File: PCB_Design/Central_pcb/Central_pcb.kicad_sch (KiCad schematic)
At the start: 12 parts, among them U3 NRF52832-QFAA-R, Y1 CX2016DB32000D0WZRC1

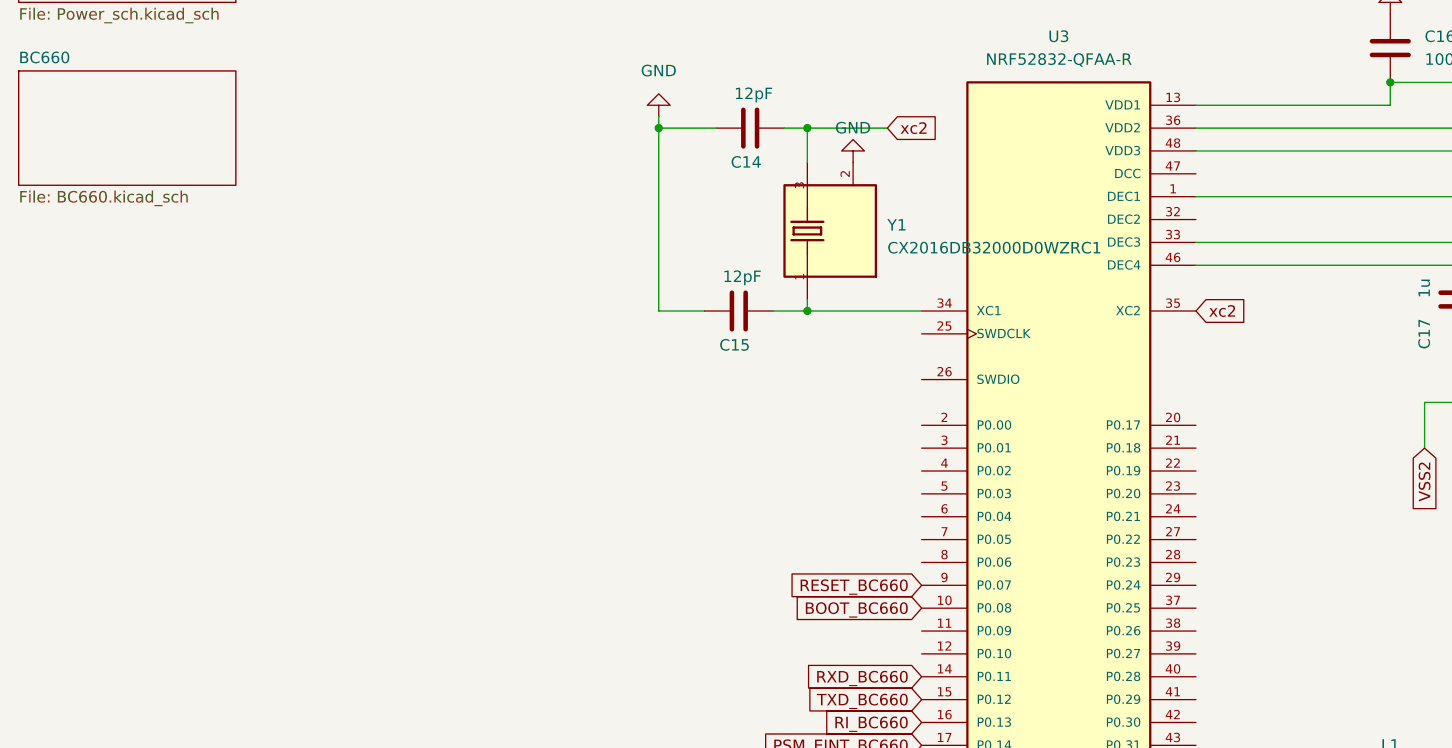
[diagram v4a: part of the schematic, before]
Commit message: Added debug conn
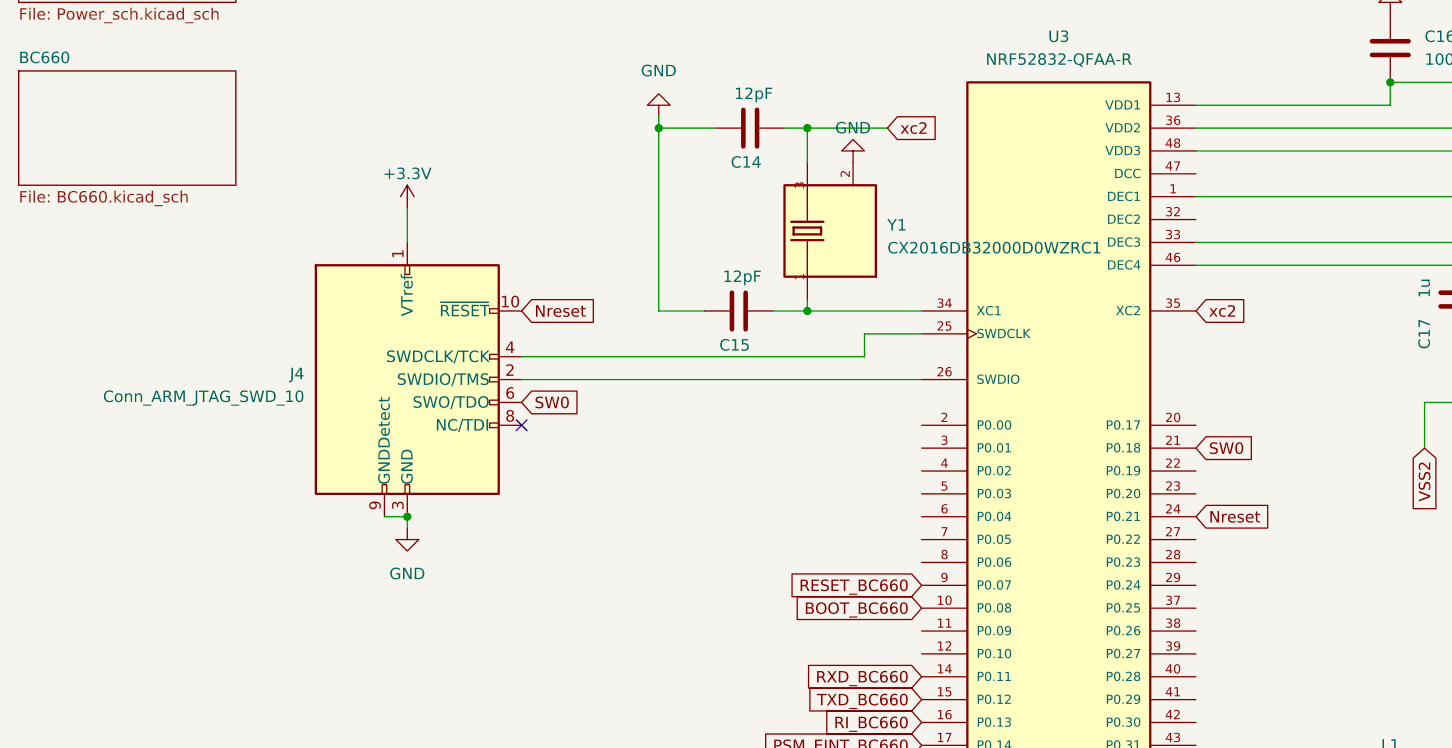
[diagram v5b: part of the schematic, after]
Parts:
- added J4: Conn_ARM_JTAG_SWD_10, Connector_PinSocket_1.27mm:PinSocket_2x05_P1.27mm_Vertical, symbol Connector:Conn_ARM_JTAG_SWD_10
- Y1: footprint CX2016DB32000D0WZRC1:OSCCC200X160X45N -> Central:OSCCC200X160X45N
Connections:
- net +3.3V: now also J4.1 (VTref)
- net GND: now also J4.3 (GND), J4.5 (GND), J4.9 (GNDDetect)
- net SW0: now reaches U3.21 (P0.18)
- net SW0: now also J4.6 (SWO/TDO)
- net Nreset: now reaches U3.24 (P0.21)
- net Nreset: now also J4.10 (~{RESET})
- net at U3.25 (SWDCLK): now also J4.4 (SWDCLK/TCK)
- net at U3.26 (SWDIO): now also J4.2 (SWDIO/TMS)
- no-connect marks 0 -> 1
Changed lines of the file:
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@@
   (junction (at 171.45 130.81) (diameter 0) (color 0 0 0 0)
   )
+  (junction (at 69.85 90.17) (diameter 0) (color 0 0 0 0)
+  )
+  (no_connect (at 82.55 80.01))
   (wire (pts (xy 208.28 53.34) (xy 203.2 53.34))
     (stroke (width 0) (type default))
@@
     (stroke (width 0) (type default))
   )
+  (wire (pts (xy 69.85 55.88) (xy 69.85 59.69))
+    (stroke (width 0) (type default))
+  )
   (wire (pts (xy 114.3 67.31) (xy 110.49 67.31))
     (stroke (width 0) (type default))
@@
     (stroke (width 0) (type default))
   )
+  (wire (pts (xy 69.85 90.17) (xy 69.85 91.44))
+    (stroke (width 0) (type default))
+  )
   (wire (pts (xy 187.96 54.61) (xy 157.48 54.61))
     (stroke (width 0) (type default))
   )
+  (wire (pts (xy 120.65 72.39) (xy 120.65 69.85))
+    (stroke (width 0) (type default))
+  )
   (wire (pts (xy 114.3 66.04) (xy 114.3 67.31))
     (stroke (width 0) (type default))
@@
     (stroke (width 0) (type default))
   )
+  (wire (pts (xy 67.31 90.17) (xy 69.85 90.17))
+    (stroke (width 0) (type default))
+  )
   (wire (pts (xy 182.88 77.47) (xy 182.88 82.55))
     (stroke (width 0) (type default))
@@
     (stroke (width 0) (type default))
   )
+  (wire (pts (xy 82.55 74.93) (xy 127 74.93))
+    (stroke (width 0) (type default))
+  )
   (wire (pts (xy 186.69 69.85) (xy 186.69 77.47))
     (stroke (width 0) (type default))
   )
+  (wire (pts (xy 120.65 69.85) (xy 127 69.85))
+    (stroke (width 0) (type default))
+  )
   (wire (pts (xy 171.45 132.08) (xy 171.45 130.81))
     (stroke (width 0) (type default))
@@
   )
   (wire (pts (xy 97.79 46.99) (xy 97.79 67.31))
+    (stroke (width 0) (type default))
+  )
+  (wire (pts (xy 82.55 72.39) (xy 120.65 72.39))
     (stroke (width 0) (type default))
   )
@@
     )
   )
+  (global_label "Nreset" (shape input) (at 157.48 90.17 0) (fields_autoplaced)
+    (effects (font (size 1.27 1.27)) (justify left))
+    (property "Intersheetrefs" "${INTERSHEET_REFS}" (at 166.4335 90.17 0)
+      (effects (font (size 1.27 1.27)) (justify left) hide)
+    )
+  )
+  (global_label "Nreset" (shape input) (at 82.55 67.31 0) (fields_autoplaced)
+    (effects (font (size 1.27 1.27)) (justify left))
+    (property "Intersheetrefs" "${INTERSHEET_REFS}" (at 91.5035 67.31 0)
+      (effects (font (size 1.27 1.27)) (justify left) hide)
+    )
+  )
+  (global_label "SW0" (shape input) (at 82.55 77.47 0) (fields_autoplaced)
+    (effects (font (size 1.27 1.27)) (justify left))
+    (property "Intersheetrefs" "${INTERSHEET_REFS}" (at 89.3262 77.47 0)
+      (effects (font (size 1.27 1.27)) (justify left) hide)
+    )
+  )
   (global_label "xc2" (shape input) (at 157.48 67.31 0) (fields_autoplaced)
     (effects (font (size 1.27 1.27)) (justify left))
     (property "Intersheetrefs" "${INTERSHEET_REFS}" (at 163.7914 67.31 0)
+      (effects (font (size 1.27 1.27)) (justify left) hide)
+    )
+  )
+  (global_label "SW0" (shape input) (at 157.48 82.55 0) (fields_autoplaced)
+    (effects (font (size 1.27 1.27)) (justify left))
+    (property "Intersheetrefs" "${INTERSHEET_REFS}" (at 164.2562 82.55 0)
       (effects (font (size 1.27 1.27)) (justify left) hide)
     )
@@
     )
   )
+  (symbol (lib_id "power:GND") (at 69.85 91.44 0) (unit 1)
+    (in_bom yes) (on_board yes) (dnp no) (fields_autoplaced)
+    (property "Reference" "#PWR037" (at 69.85 97.79 0)
+      (effects (font (size 1.27 1.27)) hide)
+    )
+    (property "Value" "GND" (at 69.85 96.52 0)
+      (effects (font (size 1.27 1.27)))
+    )
+    (property "Footprint" "" (at 69.85 91.44 0)
+      (effects (font (size 1.27 1.27)) hide)
+    )
+    (property "Datasheet" "" (at 69.85 91.44 0)
+      (effects (font (size 1.27 1.27)) hide)
+    )
+    (pin "1")
+    (instances
+      (project "Central_pcb"
+        (path "/4d244925-fc91-48ed-8daa-e4f0d6afeb7f"
+          (reference "#PWR037") (unit 1)
+        )
+      )
+    )
+  )
   (symbol (lib_id "power:GND") (at 119.38 50.8 180) (unit 1)
     (in_bom yes) (on_board yes) (dnp no) (fields_autoplaced)
@@
         (path "/4d244925-fc91-48ed-8daa-e4f0d6afeb7f"
           (reference "#PWR027") (unit 1)
+        )
+      )
+    )
+  )
+  (symbol (lib_id "power:+3.3V") (at 69.85 55.88 0) (unit 1)
+    (in_bom yes) (on_board yes) (dnp no) (fields_autoplaced)
+    (property "Reference" "#PWR036" (at 69.85 59.69 0)
+      (effects (font (size 1.27 1.27)) hide)
+    )
+    (property "Value" "+3.3V" (at 69.85 52.07 0)
+      (effects (font (size 1.27 1.27)))
+    )
+    (property "Footprint" "" (at 69.85 55.88 0)
+      (effects (font (size 1.27 1.27)) hide)
+    )
+    (property "Datasheet" "" (at 69.85 55.88 0)
+      (effects (font (size 1.27 1.27)) hide)
+    )
+    (pin "1")
+    (instances
+      (project "Central_pcb"
+        (path "/4d244925-fc91-48ed-8daa-e4f0d6afeb7f"
+          (reference "#PWR036") (unit 1)
         )
       )
@@
     )
   )
+  (symbol (lib_id "Connector:Conn_ARM_JTAG_SWD_10") (at 69.85 74.93 0) (unit 1)
+    (in_bom yes) (on_board yes) (dnp no) (fields_autoplaced)
+    (property "Reference" "J4" (at 58.42 74.295 0)
+      (effects (font (size 1.27 1.27)) (justify right))
+    )
+    (property "Value" "Conn_ARM_JTAG_SWD_10" (at 58.42 76.835 0)
+      (effects (font (size 1.27 1.27)) (justify right))
+    )
+    (property "Footprint" "Connector_PinSocket_1.27mm:PinSocket_2x05_P1.27mm_Vertical" (at 69.85 74.93 0)
+      (effects (font (size 1.27 1.27)) hide)
+    )
+    (property "Datasheet" "http://infocenter.arm.com/help/topic/com.arm.doc.ddi0314h/DDI0314H_coresight_components_trm.pdf" (at 60.96 106.68 90)
+      (effects (font (size 1.27 1.27)) hide)
+    )
+    (pin "1")
+    (pin "10")
+    (pin "2")
+    (pin "3")
+    (pin "4")
+    (pin "5")
+    (pin "6")
+    (pin "7")
+    (pin "8")
+    (pin "9")
+    (instances
+      (project "Central_pcb"
+        (path "/4d244925-fc91-48ed-8daa-e4f0d6afeb7f"
+          (reference "J4") (unit 1)
+        )
+      )
+    )
+  )
   (symbol (lib_id "Device:C") (at 179.07 38.1 180) (unit 1)
     (in_bom yes) (on_board yes) (dnp no) (fields_autoplaced)
@@
       (effects (font (size 1.27 1.27)) (justify right))
     )
-    (property "Footprint" "CX2016DB32000D0WZRC1:OSCCC200X160X45N" (at 116.84 58.42 0)
-      (effects (font (size 1.27 1.27)) (justify bottom) hide)
-    )
+    (property "Footprint" "Central:OSCCC200X160X45N" (at 116.84 58.42 0)
+      (effects (font (size 1.27 1.27)) (justify bottom) hide)
+    )

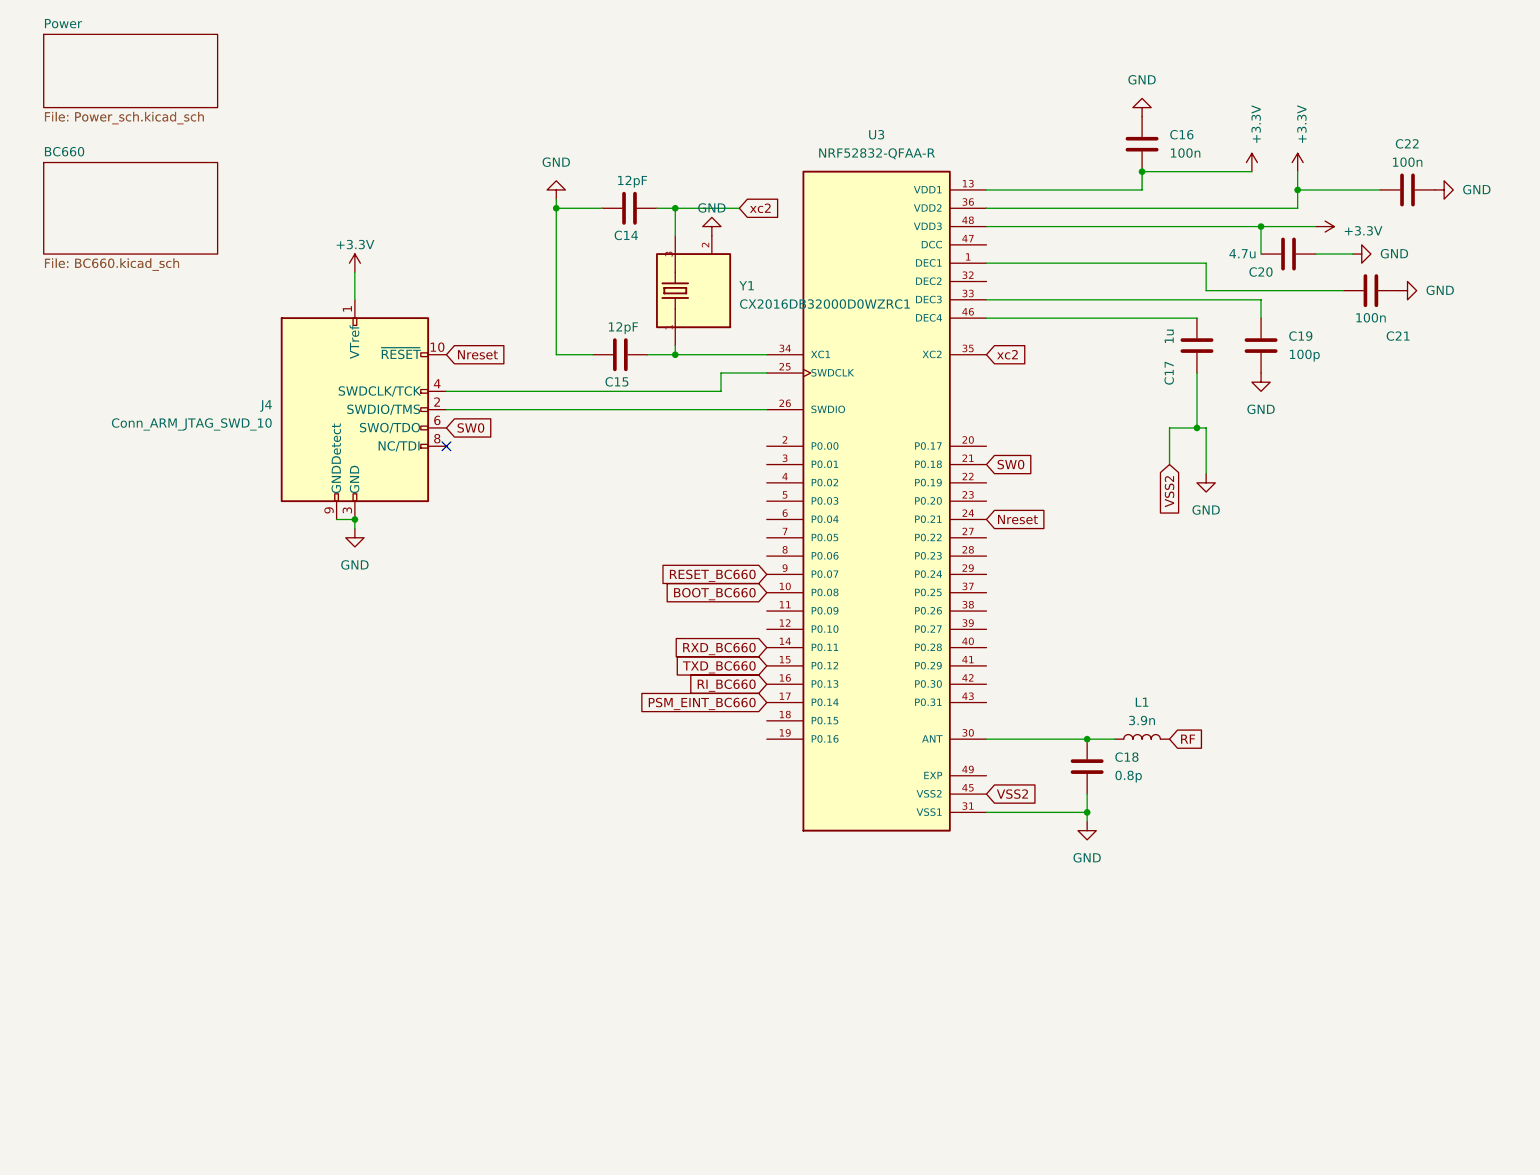
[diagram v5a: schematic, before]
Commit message: Initial PCB design
Rough sketch of what the layout could be
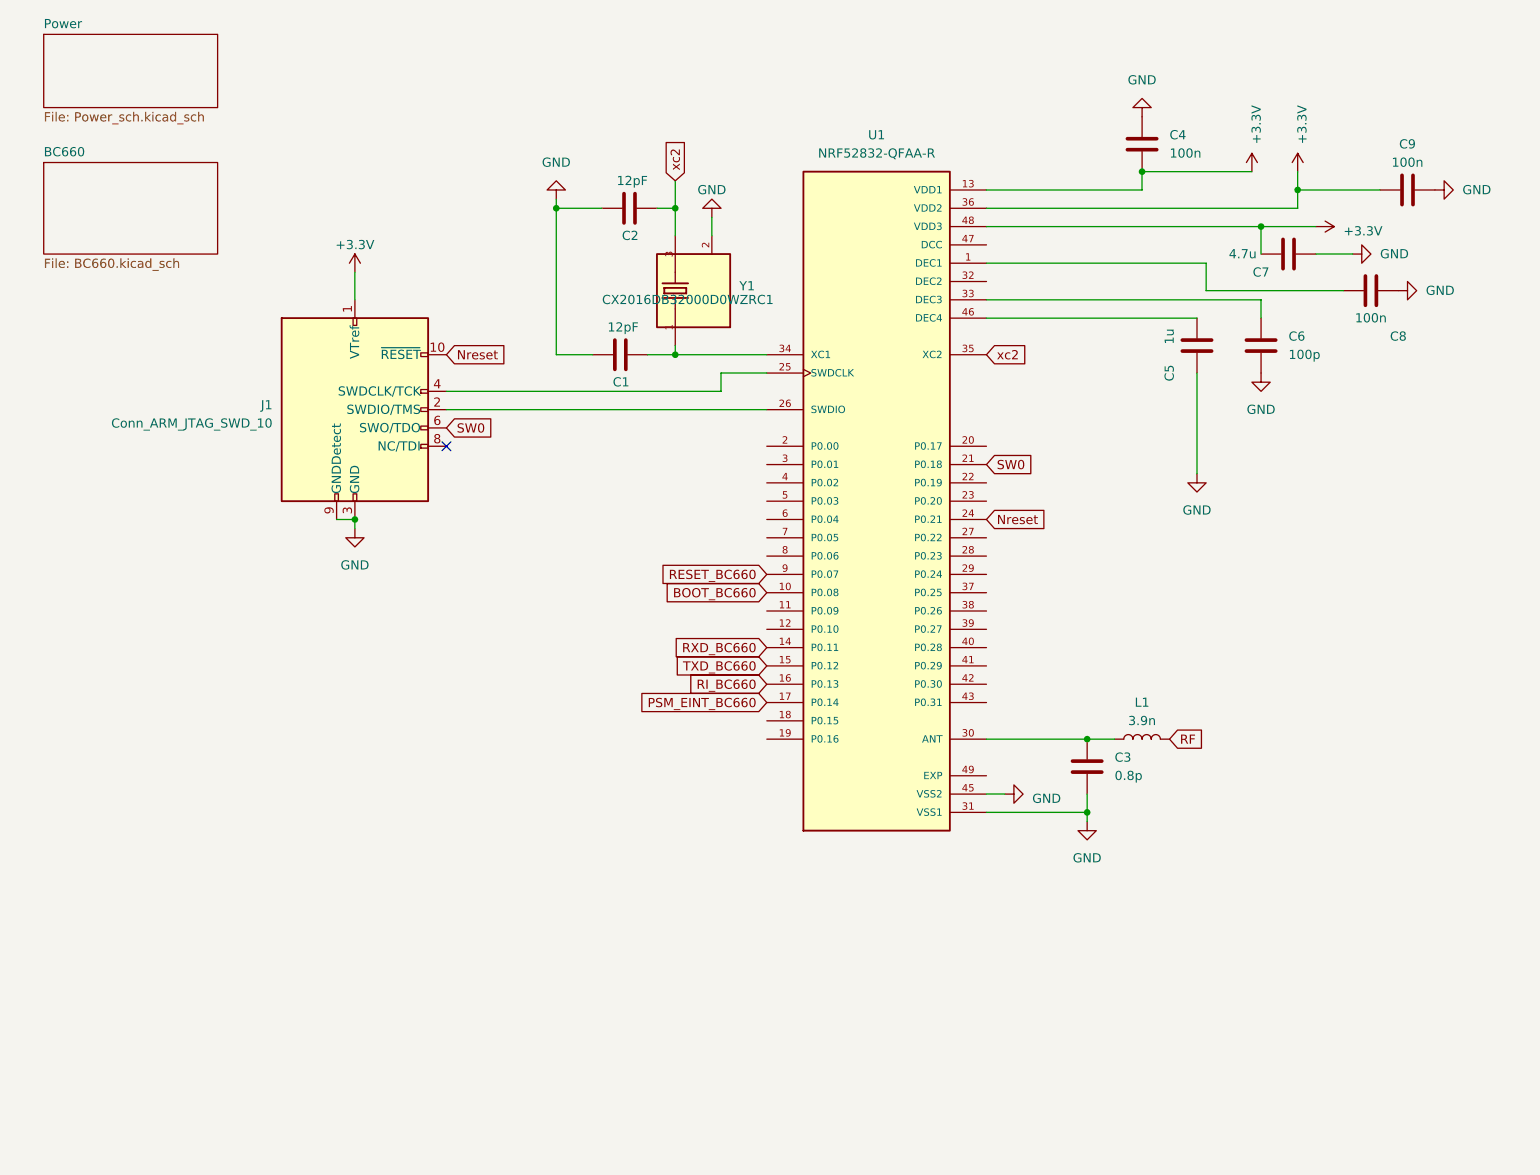
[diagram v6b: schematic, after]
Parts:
- C1: renamed from C15; footprint (none) -> Capacitor_SMD:C_0805_2012Metric_Pad1.18x1.45mm_HandSolder
- C2: renamed from C14; footprint (none) -> Capacitor_SMD:C_0805_2012Metric_Pad1.18x1.45mm_HandSolder
- C3: renamed from C18; footprint (none) -> Capacitor_SMD:C_0805_2012Metric_Pad1.18x1.45mm_HandSolder
- C4: renamed from C16; footprint (none) -> Capacitor_SMD:C_0805_2012Metric_Pad1.18x1.45mm_HandSolder
- C5: renamed from C17; footprint (none) -> Capacitor_SMD:C_0805_2012Metric_Pad1.18x1.45mm_HandSolder
- C6: renamed from C19; footprint (none) -> Capacitor_SMD:C_0805_2012Metric_Pad1.18x1.45mm_HandSolder
- C7: renamed from C20; footprint (none) -> Capacitor_SMD:C_0805_2012Metric_Pad1.18x1.45mm_HandSolder
- C8: renamed from C21; footprint (none) -> Capacitor_SMD:C_0805_2012Metric_Pad1.18x1.45mm_HandSolder
- C9: renamed from C22; footprint (none) -> Capacitor_SMD:C_0805_2012Metric_Pad1.18x1.45mm_HandSolder
- L1: footprint (none) -> Capacitor_SMD:C_0402_1005Metric_Pad0.74x0.62mm_HandSolder
- renumbered J4 to J1, U3 to U1

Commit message: PCB route
Volledig geroute nog juist controleren en mounting holes doen + controleren dat er overal gnd en 3.3v mooi verbonden is
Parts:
- added C23: 1.2pF, Capacitor_SMD:C_0805_2012Metric_Pad1.18x1.45mm_HandSolder, symbol Device:C
- added J4: U.FL-R-SMT_01_, Central:HRS_U.FL-R-SMT_01_, symbol UFL:U.FL-R-SMT_01_
- C3: footprint Capacitor_SMD:C_0805_2012Metric_Pad1.18x1.45mm_HandSolder -> Capacitor_SMD:C_0603_1608Metric_Pad1.08x0.95mm_HandSolder
- L1: footprint Capacitor_SMD:C_0402_1005Metric_Pad0.74x0.62mm_HandSolder -> Capacitor_SMD:C_0805_2012Metric_Pad1.18x1.45mm_HandSolder
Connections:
- net BOOT_BC660: now also U1.39 (P0.27); no longer U1.10 (P0.08)
- net GND: now also U1.49 (EXP), C23.1, J4.1 (GND), J4.2 (GND)
- net PSM_EINT_BC660: now also U1.10 (P0.08); no longer U1.17 (P0.14)
- net RI_BC660: now also U1.11 (P0.09); no longer U1.16 (P0.13)
- net RF: no longer names the net of L1.2
- net RF: now also C23.2, J4.3 (SIG)
- no-connect marks 1 -> 27
